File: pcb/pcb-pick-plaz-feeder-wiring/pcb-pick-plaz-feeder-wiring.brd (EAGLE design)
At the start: 40 x 60 mm, 15 parts, among them J1 03-JST-B3B-XH-A, J2 03-JST-B3B-XH-A, J3 03-JST-B3B-XH-A, J4 03-JST-B3B-XH-A, J5 02-JST-B3B-XH-A, J6 05-JST-B5B-XH-A

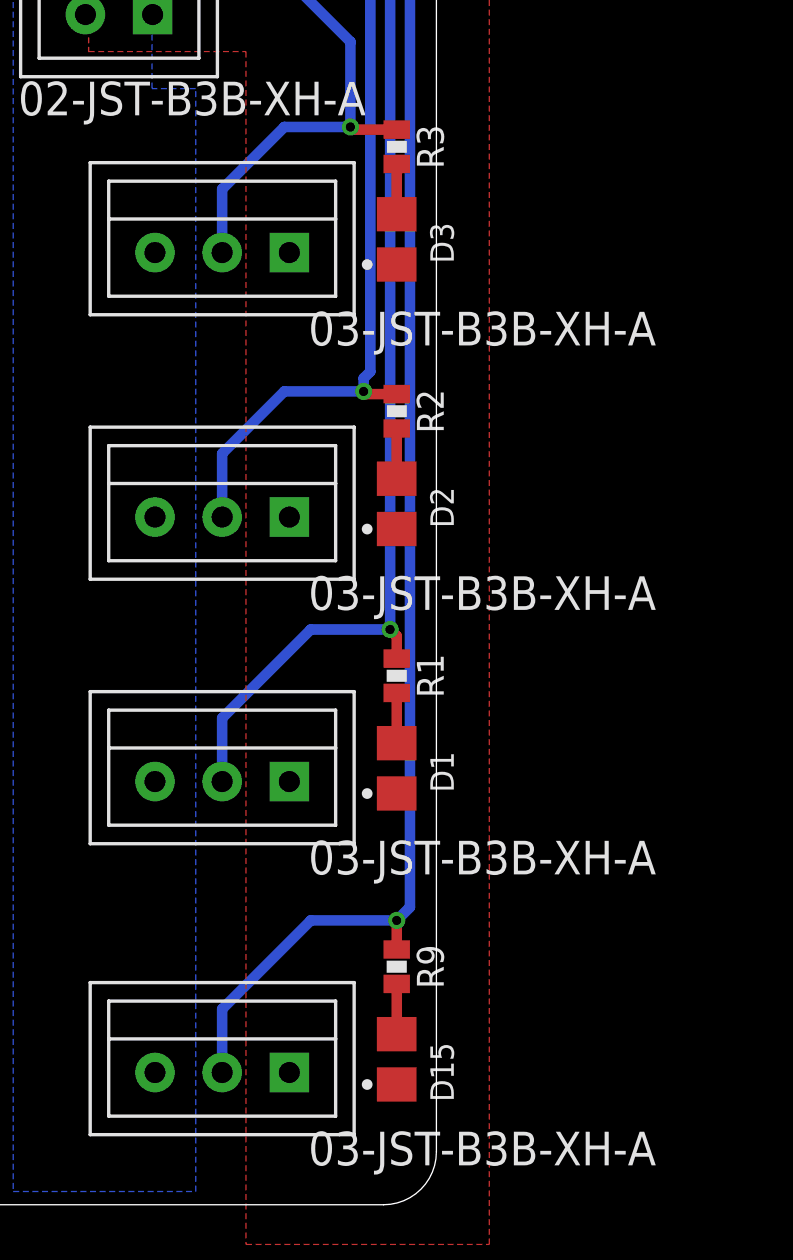
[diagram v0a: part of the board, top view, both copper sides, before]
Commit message: updated pcbs with step files
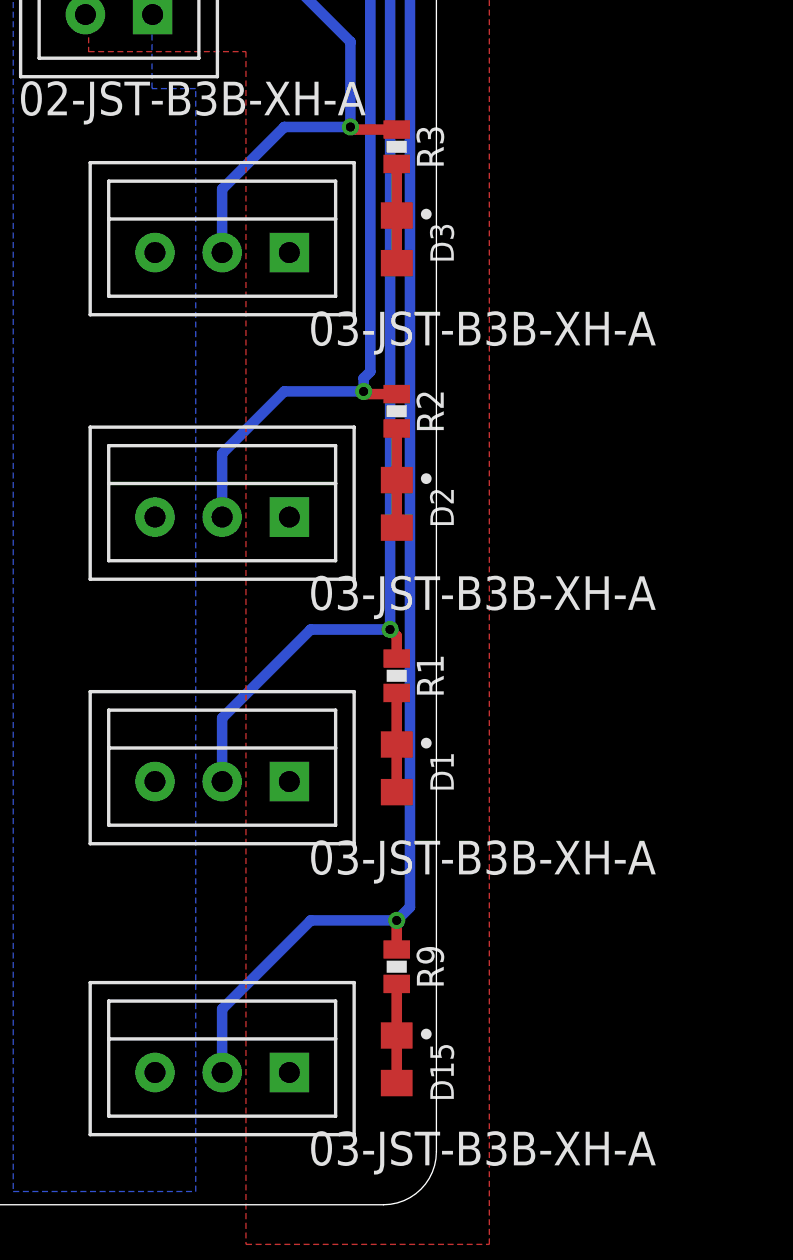
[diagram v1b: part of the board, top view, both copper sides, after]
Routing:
- net N$8: track 1.90 -> 3.75 mm
- net N$6: track 1.90 -> 3.75 mm
- net N$3: track 1.90 -> 3.75 mm
- net N$7: track 1.90 -> 3.75 mm
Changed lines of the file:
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@@
 <drawing>
 <settings>
-<setting alwaysvectorfont="yes"/>
+<setting alwaysvectorfont="no"/>
 <setting verticaltext="up"/>
 </settings>
@@
 <attribute name="VALUE" x="36.88" y="57.81" size="1.27" layer="21" rot="R180"/>
 </element>
-<element name="D15" library="ftobler" package="0805-DOT" value="LED-0805" x="38.5" y="5.5" smashed="yes" rot="R270">
+<element name="D15" library="ftobler" package="0805-DOT" package3d_urn="urn:adsk.eagle:package:36806138/4" value="LED-0805" x="38.5" y="5.5" smashed="yes" rot="R270">
 <attribute name="NAME" x="39.77" y="6.135" size="0.889" layer="25" rot="R270"/>
 <attribute name="VALUE" x="35.96" y="6.135" size="0.889" layer="27" rot="R270"/>
 </element>
-<element name="R9" library="passives" package="0603-RES" value="1k" x="38.5" y="9" smashed="yes" rot="R270">
+<element name="R9" library="passives" package="0603-RES" package3d_urn="urn:adsk.eagle:package:36812383/4" value="1k" x="38.5" y="9" smashed="yes" rot="R270">
 <attribute name="NAME" x="39.262" y="9" size="1.016" layer="25" font="vector" ratio="12" rot="R270" align="bottom-center"/>
 </element>
-<element name="D1" library="ftobler" package="0805-DOT" value="LED-0805" x="38.5" y="16.5" smashed="yes" rot="R270">
+<element name="D1" library="ftobler" package="0805-DOT" package3d_urn="urn:adsk.eagle:package:36806138/4" value="LED-0805" x="38.5" y="16.5" smashed="yes" rot="R270">
 <attribute name="NAME" x="39.77" y="17.135" size="0.889" layer="25" rot="R270"/>
 <attribute name="VALUE" x="35.96" y="17.135" size="0.889" layer="27" rot="R270"/>
 </element>
-<element name="R1" library="passives" package="0603-RES" value="1k" x="38.5" y="20" smashed="yes" rot="R270">
+<element name="R1" library="passives" package="0603-RES" package3d_urn="urn:adsk.eagle:package:36812383/4" value="1k" x="38.5" y="20" smashed="yes" rot="R270">
 <attribute name="NAME" x="39.262" y="20" size="1.016" layer="25" font="vector" ratio="12" rot="R270" align="bottom-center"/>
 </element>
-<element name="D2" library="ftobler" package="0805-DOT" value="LED-0805" x="38.5" y="26.5" smashed="yes" rot="R270">
+<element name="D2" library="ftobler" package="0805-DOT" package3d_urn="urn:adsk.eagle:package:36806138/4" value="LED-0805" x="38.5" y="26.5" smashed="yes" rot="R270">
 <attribute name="NAME" x="39.77" y="27.135" size="0.889" layer="25" rot="R270"/>
 <attribute name="VALUE" x="35.96" y="27.135" size="0.889" layer="27" rot="R270"/>
 </element>
-<element name="R2" library="passives" package="0603-RES" value="1k" x="38.5" y="30" smashed="yes" rot="R270">
+<element name="R2" library="passives" package="0603-RES" package3d_urn="urn:adsk.eagle:package:36812383/4" value="1k" x="38.5" y="30" smashed="yes" rot="R270">
 <attribute name="NAME" x="39.262" y="30" size="1.016" layer="25" font="vector" ratio="12" rot="R270" align="bottom-center"/>
 </element>
-<element name="D3" library="ftobler" package="0805-DOT" value="LED-0805" x="38.5" y="36.5" smashed="yes" rot="R270">
+<element name="D3" library="ftobler" package="0805-DOT" package3d_urn="urn:adsk.eagle:package:36806138/4" value="LED-0805" x="38.5" y="36.5" smashed="yes" rot="R270">
 <attribute name="NAME" x="39.77" y="37.135" size="0.889" layer="25" rot="R270"/>
 <attribute name="VALUE" x="35.96" y="37.135" size="0.889" layer="27" rot="R270"/>
 </element>
-<element name="R3" library="passives" package="0603-RES" value="1k" x="38.5" y="40" smashed="yes" rot="R270">
+<element name="R3" library="passives" package="0603-RES" package3d_urn="urn:adsk.eagle:package:36812383/4" value="1k" x="38.5" y="40" smashed="yes" rot="R270">
 <attribute name="NAME" x="39.262" y="40" size="1.016" layer="25" font="vector" ratio="12" rot="R270" align="bottom-center"/>
 </element>
@@
 <contactref element="D2" pad="2"/>
 <contactref element="D3" pad="2"/>
+<wire x1="29.27" y1="45" x2="36.88" y2="54" width="0" layer="19" extent="1-1"/>
+<wire x1="34.44" y1="36" x2="29.27" y2="45" width="0" layer="19" extent="1-1"/>
+<wire x1="38.5" y1="37.4" x2="34.44" y2="36" width="0" layer="19" extent="1-1"/>
+<wire x1="38.5" y1="27.4" x2="34.44" y2="36" width="0" layer="19" extent="1-1"/>
+<wire x1="34.44" y1="26" x2="38.5" y2="27.4" width="0" layer="19" extent="1-1"/>
+<wire x1="38.5" y1="17.4" x2="34.44" y2="26" width="0" layer="19" extent="1-1"/>
+<wire x1="34.44" y1="16" x2="38.5" y2="17.4" width="0" layer="19" extent="1-1"/>
+<wire x1="38.5" y1="6.4" x2="34.44" y2="16" width="0" layer="19" extent="1-1"/>
+<wire x1="34.44" y1="5" x2="38.5" y2="6.4" width="0" layer="19" extent="1-1"/>
 </signal>
 <signal name="+5V">
@@
 <contactref element="D15" pad="1"/>
 <contactref element="R9" pad="2"/>
-<wire x1="38.5" y1="8.35" x2="38.5" y2="6.45" width="0.4" layer="1"/>
+<wire x1="38.5" y1="8.35" x2="38.5" y2="4.6" width="0.4" layer="1"/>
 </signal>
 <signal name="N$3">
 <contactref element="D1" pad="1"/>
 <contactref element="R1" pad="2"/>
-<wire x1="38.5" y1="19.35" x2="38.5" y2="17.45" width="0.4" layer="1"/>
+<wire x1="38.5" y1="19.35" x2="38.5" y2="15.6" width="0.4" layer="1"/>
 </signal>
 <signal name="N$7">
 <contactref element="D2" pad="1"/>
 <contactref element="R2" pad="2"/>
-<wire x1="38.5" y1="29.35" x2="38.5" y2="27.45" width="0.4" layer="1"/>
+<wire x1="38.5" y1="29.35" x2="38.5" y2="25.6" width="0.4" layer="1"/>
 </signal>
 <signal name="N$8">
 <contactref element="D3" pad="1"/>
 <contactref element="R3" pad="2"/>
-<wire x1="38.5" y1="39.35" x2="38.5" y2="37.45" width="0.4" layer="1"/>
+<wire x1="38.5" y1="39.35" x2="38.5" y2="35.6" width="0.4" layer="1"/>
 </signal>
 </signals>
